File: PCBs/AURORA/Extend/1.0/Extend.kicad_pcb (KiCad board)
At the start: 2 copper layers, 85 x 55 mm, 27 parts, among them J1 Conn_01x05_Pin, J10 Conn_01x02_Male, J11 Conn_01x02_Male, J12 Conn_01x02_Male, J13 Conn_01x04_Pin, J2 Conn_01x05_Pin, J3 Conn_01x04_Pin, J5 Conn_01x02_Male, J6 Conn_01x02_Male, J7 Conn_01x02_Pin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

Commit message: Moving files
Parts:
- removed C2: 0.1u, Capacitor_SMD:C_0805_2012Metric_Pad1.18x1.45mm_HandSolder
- removed J10, J11, J12: Conn_01x02_Male, Connector_JST:JST_PH_B2B-PH-K_1x02_P2.00mm_Vertical
- removed R4: 320R, Resistor_SMD:R_0603_1608Metric_Pad0.98x0.95mm_HandSolder
- removed U2: MCP23017_SS, Package_SO:SSOP-28_5.3x10.2mm_P0.65mm
- J1: value Conn_01x05_Pin -> Conn_01x06_Pin; footprint Connector_JST:JST_PH_B5B-PH-K_1x05_P2.00mm_Vertical -> Connector_JST:JST_PH_B6B-PH-K_1x06_P2.00mm_Vertical
- moved J7 42.5 mm to (166.0, 88.3), turned to 0 degrees
- moved R2 38.6 mm to (162.9, 88.2), turned to -90 degrees
- moved C4 31.1 mm to (160.3, 77.0), turned to 180 degrees
- moved C3 28.1 mm to (132.2, 107.1), turned to 180 degrees
- moved C1 24.7 mm to (131.6, 104.6), turned to 180 degrees
- moved U1 14.8 mm to (128.4, 96.7), turned to 90 degrees
- moved J6 6.60 mm to (168.4, 80.2)
- moved J13 5.08 mm to (141.3, 67.0)
- moved J8 4.28 mm to (89.2, 83.7)
- moved R3 4.27 mm to (95.3, 92.0)
- moved J1 3.54 mm to (123.4, 67.0)
- moved J5 2.70 mm to (89.2, 74.6)
- moved D1 0.72 mm to (168.1, 98.5)
- moved R1 0.72 mm to (168.1, 101.8)
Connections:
- J1 pad 3: DSP_NRST -> DSP_EN1
- J1 pad 4: DSP_BOOT0 -> DSP_EN2
- J1 pad 5: DSP_INT -> DSP_EN3
- U1 pad 19: INTA -> INTB
- U1 pad 20: unconnected-(U1-INTA-Pad20) -> INTA
- U1 pad 25: unconnected-(U1-GPA4-Pad25) -> DSP_EN1
- U1 pad 26: DSP_NRST -> DSP_EN2
- U1 pad 27: DSP_BOOT0 -> DSP_EN3
- U1 pad 28: DSP_INT -> DSP_BOOT
- U1 pad 6: Net-(U1-GPB5) -> SPDIF_INT1
- U1 pad 7: VOLUME_BUTTON -> SPDIF_INT2
- U1 pad 8: INPUT_BUTTON -> SPDIF_RESET
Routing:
- net GND: track 156.6 -> 0.00 mm, vias 7 -> 4
- net DSP_INT: track 36.1 -> 0.00 mm, vias 1 -> 0
- net DSP_EN3: track 0.00 -> 36.1 mm, vias 0 -> 1
- net DSP_BOOT: track 0.00 -> 35.3 mm, vias 0 -> 1
- net SPDIF_RESET: track 23.6 -> 56.1 mm
- net RESET: track 76.3 -> 44.2 mm
- net INPUT_BUTTON: track 32.1 -> 0.00 mm, vias 1 -> 0
- net SPDIF_INT2: track 25.9 -> 57.8 mm
- net SPDIF_INT1: track 28.6 -> 59.2 mm
- net DSP_EN2: track 0.00 -> 30.5 mm, vias 0 -> 1
- net DSP_EN1: track 0.00 -> 29.4 mm, vias 0 -> 1
- net VOLUME_BUTTON: track 29.4 -> 0.00 mm
- net CHANSEL4: track 35.3 -> 61.5 mm
- net CHANSEL2: track 30.4 -> 56.4 mm
- net CHANSEL3: track 32.9 -> 58.2 mm
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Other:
- board text added: "3V3_IN"
- board text removed: "INP_BTN"
- board text removed: "STBY_LED"
- board text removed: "VOL_BTN"

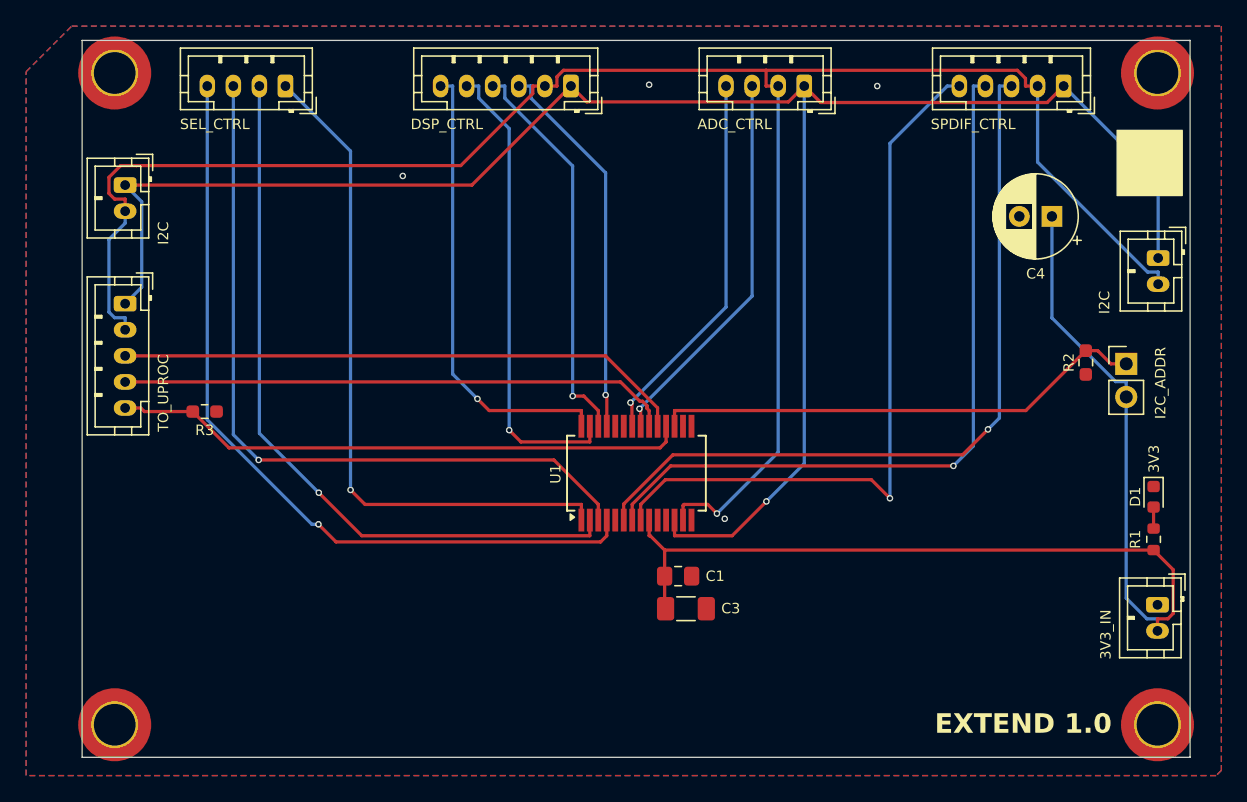
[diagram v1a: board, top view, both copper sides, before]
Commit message: Replacing PeakingEQ
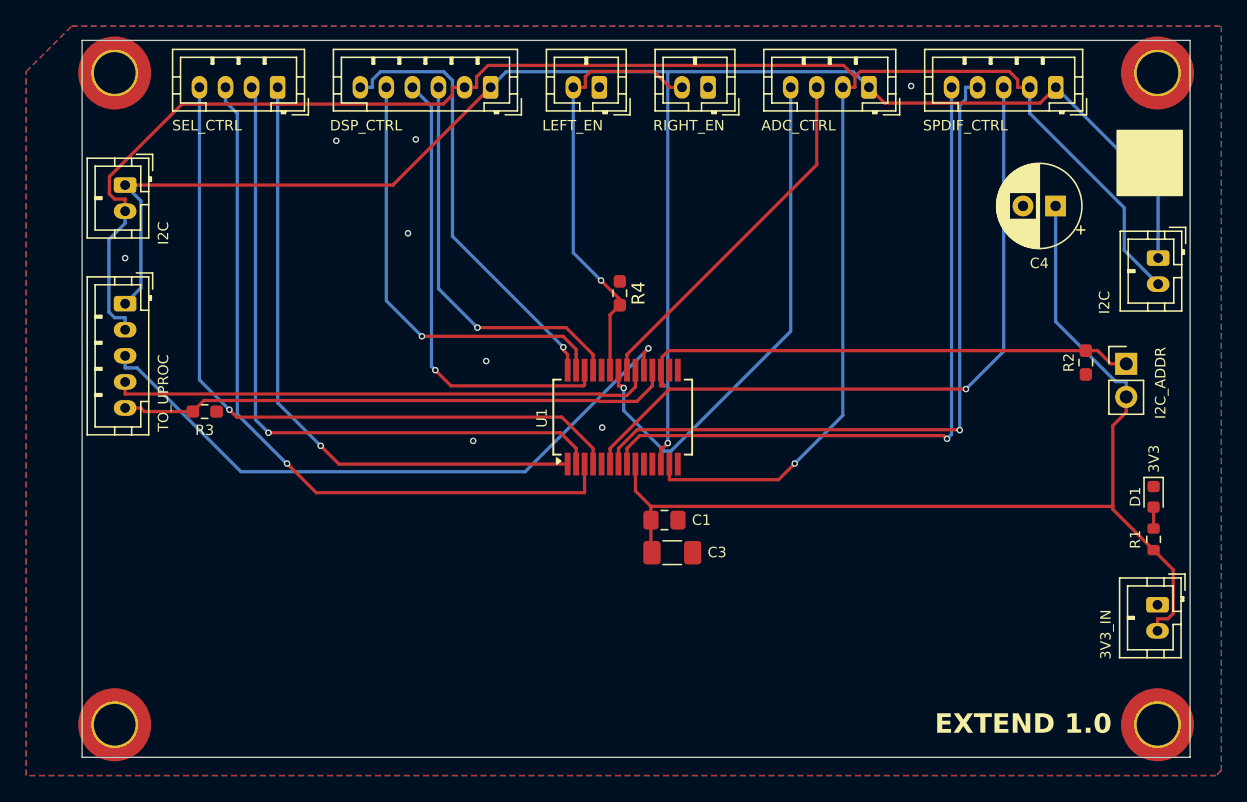
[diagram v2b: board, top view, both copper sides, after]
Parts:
- added J10: Conn_01x02_Male, Connector_JST:JST_PH_B2B-PH-K_1x02_P2.00mm_Vertical, F.Cu at (133.9, 67.1)
- added J4: Conn_01x02_Male, Connector_JST:JST_PH_B2B-PH-K_1x02_P2.00mm_Vertical, F.Cu at (125.6, 67.1)
- added R4: 4.7K, Resistor_SMD:R_0603_1608Metric_Pad0.98x0.95mm_HandSolder, F.Cu at (127.2, 82.9)
- moved J1 6.16 mm to (117.2, 67.1)
- moved J13 4.96 mm to (146.3, 67.1)
- moved C1 4.43 mm to (130.6, 100.3)
- moved U1 4.43 mm to (127.4, 92.4)
- moved C3 4.43 mm to (131.2, 102.8)
- moved C4 0.85 mm to (160.6, 76.2)
- moved J2 0.61 mm to (160.6, 67.1)
- moved J3 0.61 mm to (100.9, 67.1)
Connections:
- U1 pad 23: unconnected-(U1-GPA2-Pad23) -> MONOBLOCK_ENABLE
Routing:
- net MONOBLOCK_ENABLE: track 0.00 -> 33.3 mm, vias 0 -> 1
- net SCL: track 146.0 -> 133.4 mm
- net ADC_INT: track 29.2 -> 40.0 mm
- net 3V3: track 88.8 -> 81.4 mm
- net INTB: track 43.9 -> 50.1 mm, vias 0 -> 1
- net CHANSEL4: track 61.5 -> 56.0 mm
- net DSP_EN2: track 30.5 -> 35.5 mm
- net SPDIF_INT1: track 59.2 -> 54.7 mm
- net CHANSEL2: track 56.4 -> 52.3 mm
- net CHANSEL1: track 52.4 -> 48.4 mm
- net SPDIF_RESET: track 56.1 -> 53.4 mm
- net SPDIF_INT2: track 57.8 -> 55.4 mm
- net SDA: track 150.9 -> 153.2 mm
- net ADC_GPIO1: track 29.7 -> 27.7 mm, vias 1 -> 0
- net DSP_EN3: track 36.1 -> 34.1 mm
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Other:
- board text added: "LEFT_EN"
- board text added: "RIGHT_EN"
